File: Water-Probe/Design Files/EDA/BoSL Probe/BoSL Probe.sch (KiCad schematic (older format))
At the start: 9 parts, among them J1 8P8C_Shielded, U1 MS5803-01BA, U2 DS18B20

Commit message: commit before adding perferations to probe
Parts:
- removed J? (x2): KeyStone_Screw, Project:KeyStone_Screw, symbol Project:KeyStone_Screw
- added J2, J3: KeyStone_Screw_Small, Project:KeyStone_Screw_Small, symbol Project:KeyStone_Screw_Small
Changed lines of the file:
@@
 $EndComp
 $Comp
-L Project:KeyStone_Screw J?
-U 1 1 5D953E64
+L Project:KeyStone_Screw_Small J3
+U 1 1 5D955396
 P 8050 3100
-F 0 "J?" V 8238 3187 50  0000 L CNN
-F 1 "KeyStone_Screw" V 8327 3187 50  0000 L CNN
-F 2 "Project:KeyStone_Screw" H 8050 3100 50  0001 C CNN
-F 3 "https://docs-apac.rs-online.com/webdocs/13ec/0900766b813ecaa4.pdf" H 8050 3100 50  0001 C CNN
+F 0 "J3" V 8238 3187 50  0000 L CNN
+F 1 "KeyStone_Screw_Small" V 8327 3187 50  0000 L CNN
+F 2 "Project:KeyStone_Screw_Small" H 8050 3100 50  0001 C CNN
+F 3 "https://www.digikey.com.au/product-detail/en/keystone-electronics/7774/36-7774-ND/2745944" H 8050 3100 50  0001 C CNN
 	1    8050 3100
 	0    1    1    0
 $EndComp
 $Comp
-L Project:KeyStone_Screw J?
-U 1 1 5D9540DF
+L Project:KeyStone_Screw_Small J2
+U 1 1 5D955623
 P 7500 3100
-F 0 "J?" V 7688 3187 50  0000 L CNN
-F 1 "KeyStone_Screw" V 7777 3187 50  0000 L CNN
-F 2 "Project:KeyStone_Screw" H 7500 3100 50  0001 C CNN
-F 3 "https://docs-apac.rs-online.com/webdocs/13ec/0900766b813ecaa4.pdf" H 7500 3100 50  0001 C CNN
+F 0 "J2" V 7688 3187 50  0000 L CNN
+F 1 "KeyStone_Screw_Small" V 7777 3187 50  0000 L CNN
+F 2 "Project:KeyStone_Screw_Small" H 7500 3100 50  0001 C CNN
+F 3 "https://www.digikey.com.au/product-detail/en/keystone-electronics/7774/36-7774-ND/2745944" H 7500 3100 50  0001 C CNN
 	1    7500 3100
 	0    1    1    0

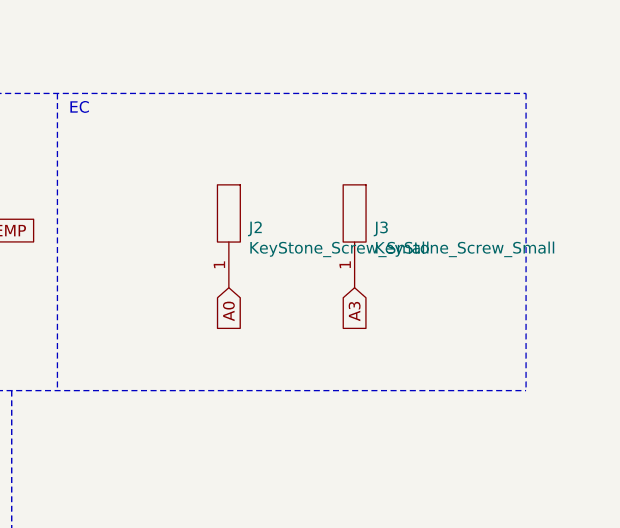
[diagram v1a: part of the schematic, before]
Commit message: changed probe EC footprint to screw terminal cleaned up bosl GPS code
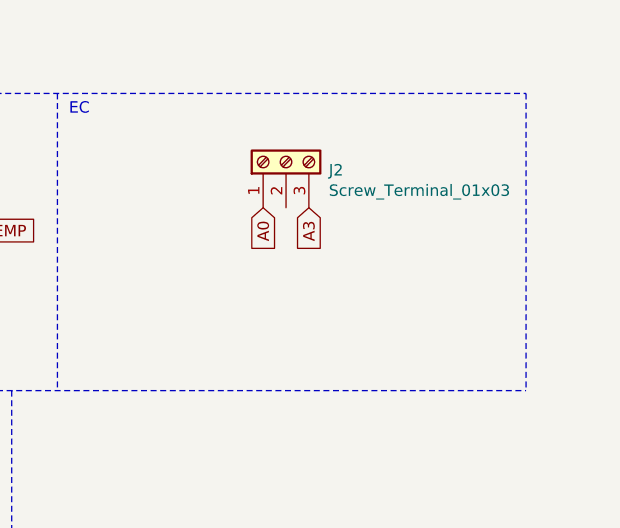
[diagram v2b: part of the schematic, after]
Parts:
- removed J2, J3: KeyStone_Screw_Small, Project:KeyStone_Screw_Small, symbol Project:KeyStone_Screw_Small
- added J2: Screw_Terminal_01x03, Project:Screw_Terminals_1x3, symbol Connector:Screw_Terminal_01x03
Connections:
- net A0: now also J2.1 (Pin_1)
- net A3: now also J2.3 (Pin_3)
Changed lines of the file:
@@
 	1    0    0    -1
 $EndComp
-Text GLabel 7500 3550 3    50   Input ~ 0
+Text GLabel 7650 3200 3    50   Input ~ 0
 A0
-Text GLabel 8050 3550 3    50   Input ~ 0
+Text GLabel 7850 3200 3    50   Input ~ 0
 A3
 Wire Notes Line
@@
 $EndComp
 $Comp
-L Project:KeyStone_Screw_Small J3
-U 1 1 5D955396
-P 8050 3100
-F 0 "J3" V 8238 3187 50  0000 L CNN
-F 1 "KeyStone_Screw_Small" V 8327 3187 50  0000 L CNN
-F 2 "Project:KeyStone_Screw_Small" H 8050 3100 50  0001 C CNN
-F 3 "https://www.digikey.com.au/product-detail/en/keystone-electronics/7774/36-7774-ND/2745944" H 8050 3100 50  0001 C CNN
-	1    8050 3100
-	0    1    1    0
-$EndComp
-$Comp
-L Project:KeyStone_Screw_Small J2
-U 1 1 5D955623
-P 7500 3100
-F 0 "J2" V 7688 3187 50  0000 L CNN
-F 1 "KeyStone_Screw_Small" V 7777 3187 50  0000 L CNN
-F 2 "Project:KeyStone_Screw_Small" H 7500 3100 50  0001 C CNN
-F 3 "https://www.digikey.com.au/product-detail/en/keystone-electronics/7774/36-7774-ND/2745944" H 7500 3100 50  0001 C CNN
-	1    7500 3100
-	0    1    1    0
+L Connector:Screw_Terminal_01x03 J2
+U 1 1 5DCE746A
+P 7750 3000
+F 0 "J2" V 7714 2813 50  0000 R CNN
+F 1 "Screw_Terminal_01x03" V 7625 2813 50  0000 R CNN
+F 2 "Project:Screw_Terminals_1x3" H 7750 3000 50  0001 C CNN
+F 3 "~" H 7750 3000 50  0001 C CNN
+	1    7750 3000
+	0    -1   -1   0
 $EndComp
 $EndSCHEMATC

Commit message: transmit code added to gps
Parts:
- J2: footprint Project:Screw_Terminals_1x3 -> Project:Screw_Terminals_1x3_3.5mm
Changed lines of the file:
@@
 F 0 "J2" V 7714 2813 50  0000 R CNN
 F 1 "Screw_Terminal_01x03" V 7625 2813 50  0000 R CNN
-F 2 "Project:Screw_Terminals_1x3" H 7750 3000 50  0001 C CNN
+F 2 "Project:Screw_Terminals_1x3_3.5mm" H 7750 3000 50  0001 C CNN
 F 3 "~" H 7750 3000 50  0001 C CNN
 	1    7750 3000

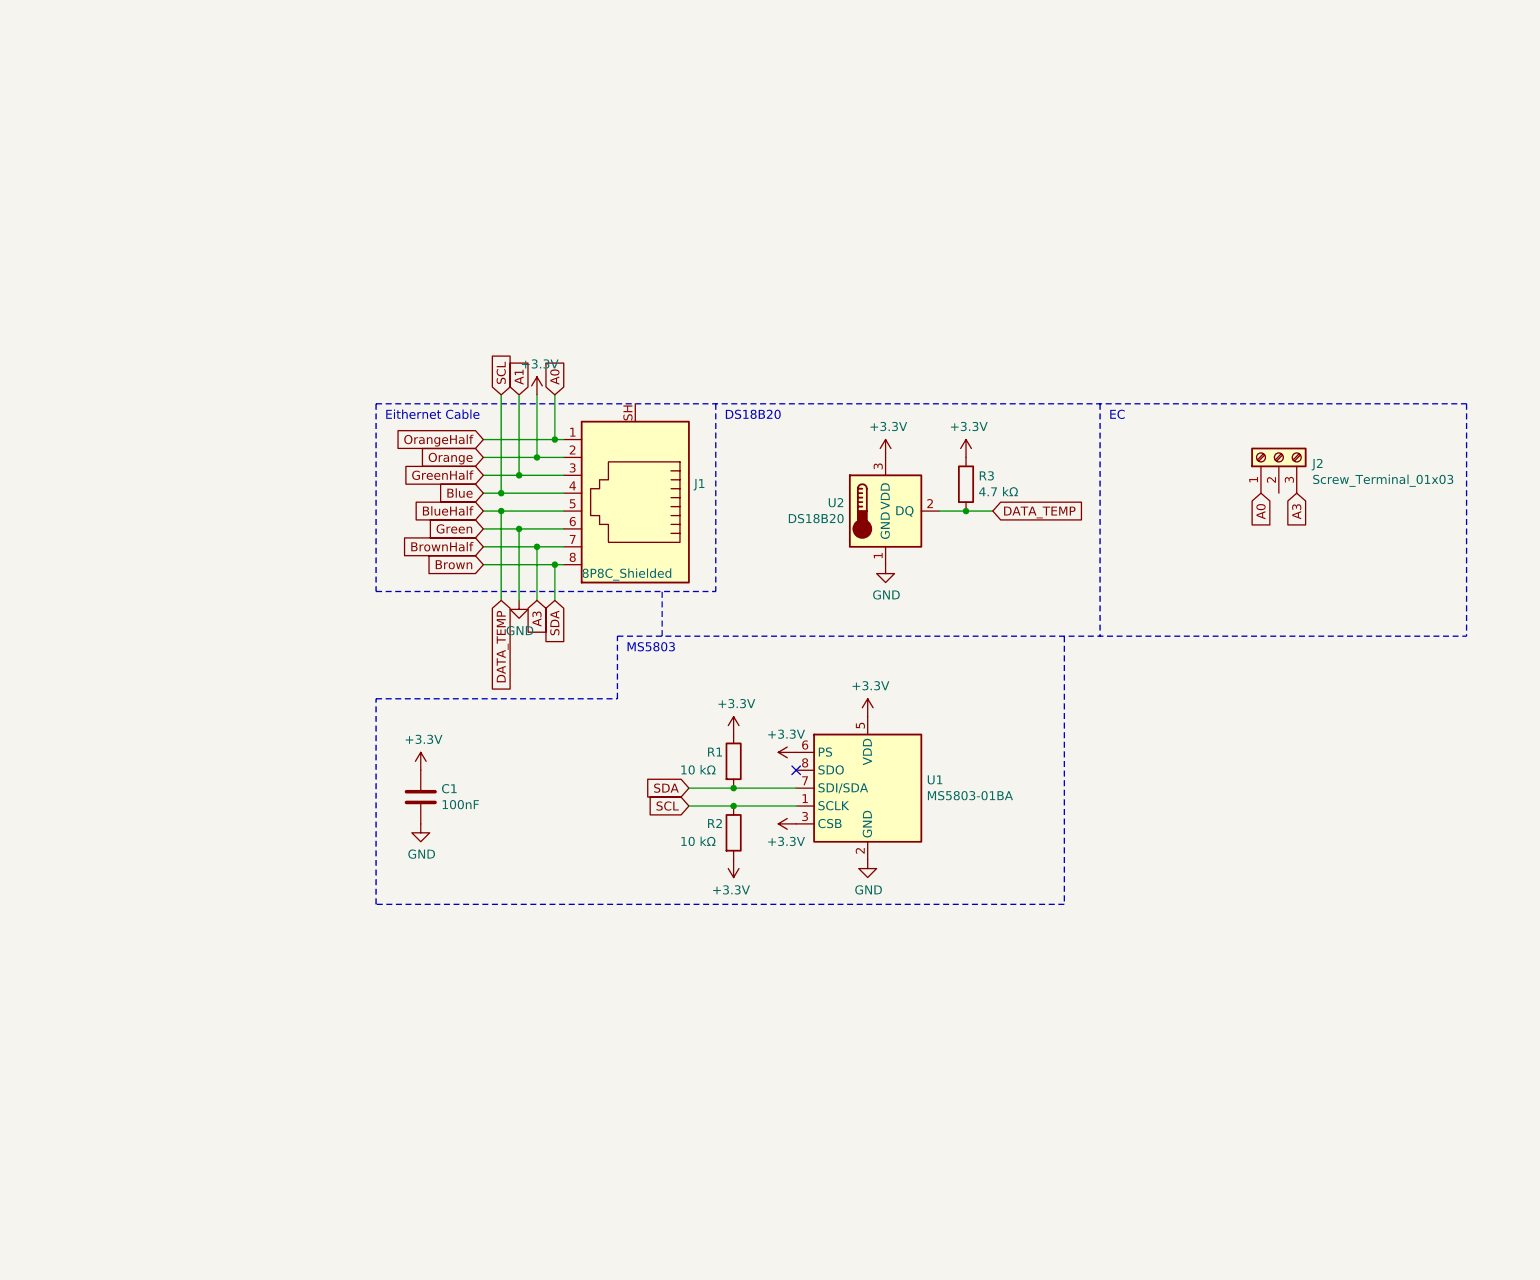
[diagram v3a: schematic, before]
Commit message: Added changes to velocity small tranducer casing based on test fitting and mounting needs for field testing
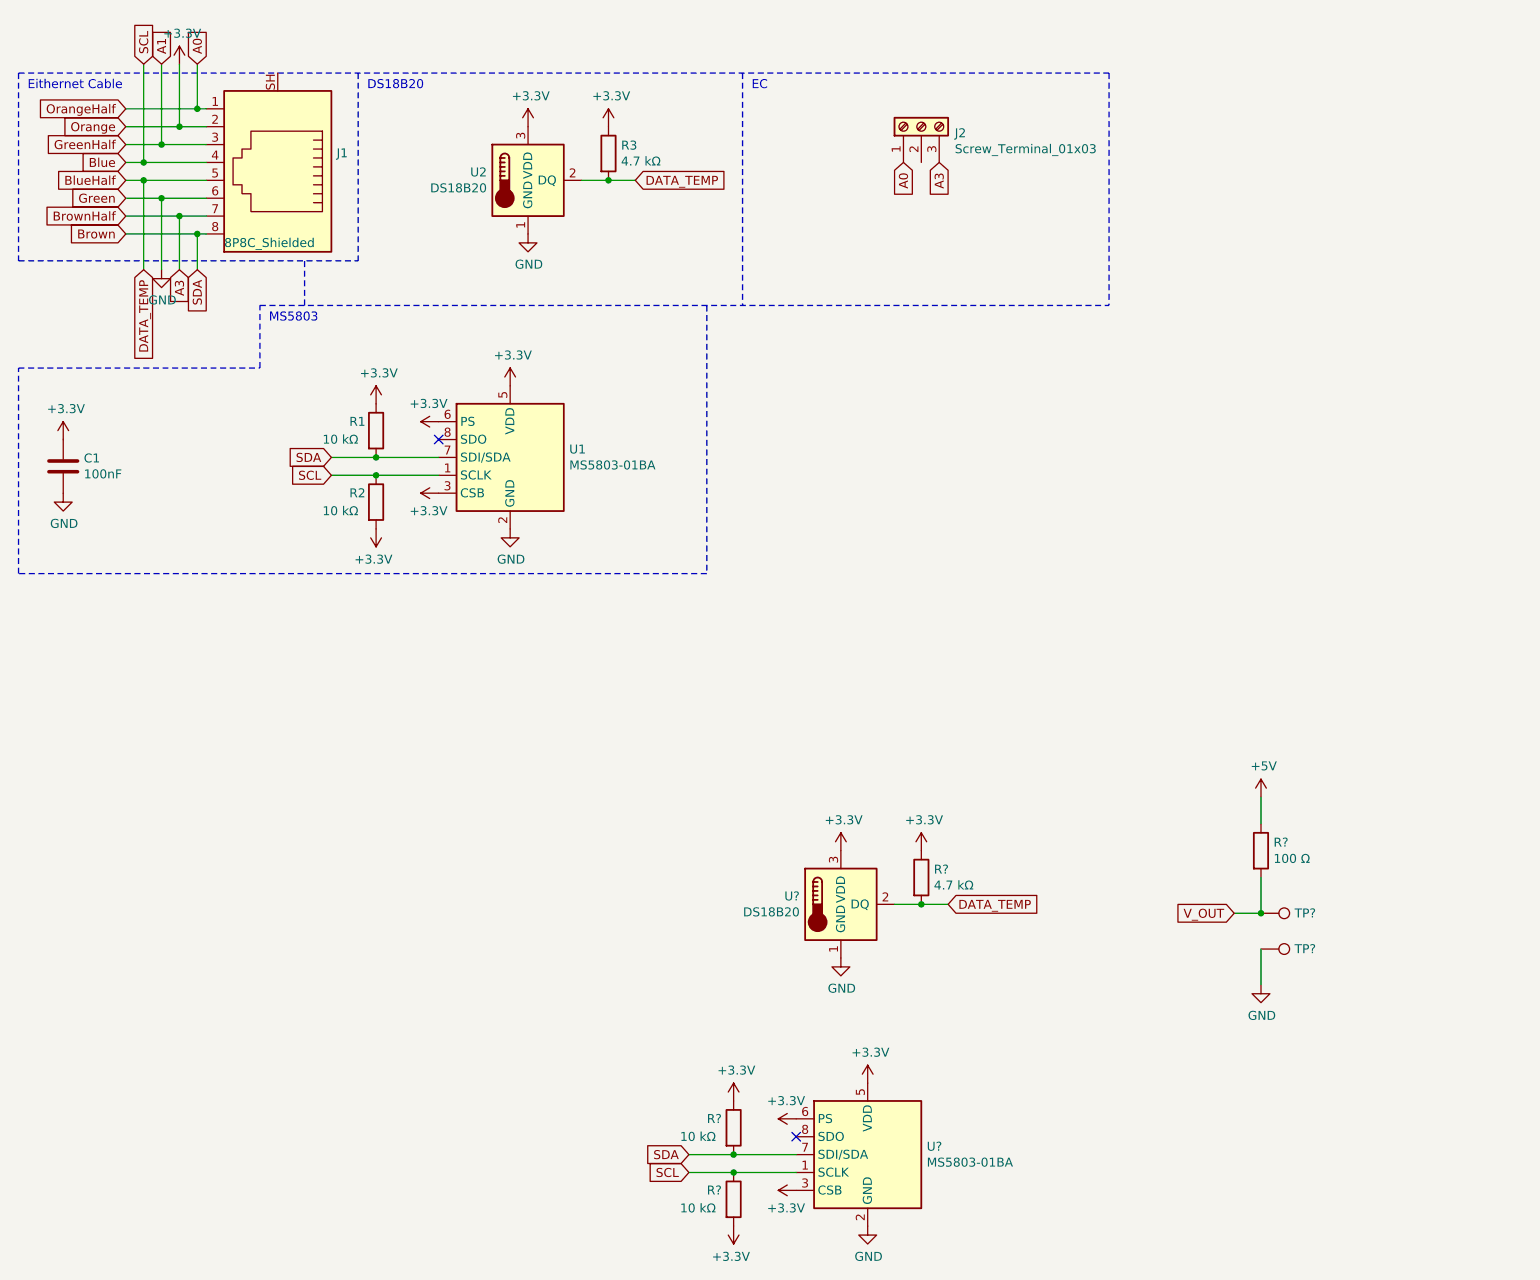
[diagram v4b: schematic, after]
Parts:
- added R? (x2): 10 kΩ, Resistors_SMD:R_0805_HandSoldering, symbol Device:R
- added R?: 4.7 kΩ, Resistors_SMD:R_0805_HandSoldering, symbol Device:R
- added R?: 100 Ω, symbol Device:R
- added TP? (x2): TestPoint, symbol Connector:TestPoint
- added U?: MS5803-01BA, Project:MS5803, symbol Project:MS5803-01BA
- added U?: DS18B20, TO_SOT_Packages_THT:TO-92_Horizontal2_Inline_Narrow_Oval, symbol Sensor_Temperature:DS18B20
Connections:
- net +3V3: now also R?.1, R?.1, R?.2, U?.3 (CSB), U?.3 (VDD), U?.5 (VDD), U?.6 (PS)
- net Blue: now also R?.1, U?.1 (SCLK)
- net BlueHalf: now also R?.2, U?.2 (DQ)
- net Brown: now also R?.2, U?.7 (SDI/SDA)
- net GND: now also TP?.1, U?.1 (GND), U?.2 (GND)
- new net +5V: R?.1
- new net V_OUT: R?.2, TP?.1
- no-connect marks 1 -> 2
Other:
- moved on the sheet: C1, J1, J2, R1, R2, R3, U1, U2
